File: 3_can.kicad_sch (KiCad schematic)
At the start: 6 parts, among them J301 Conn_01x04_Male, U301 TJA1441AT

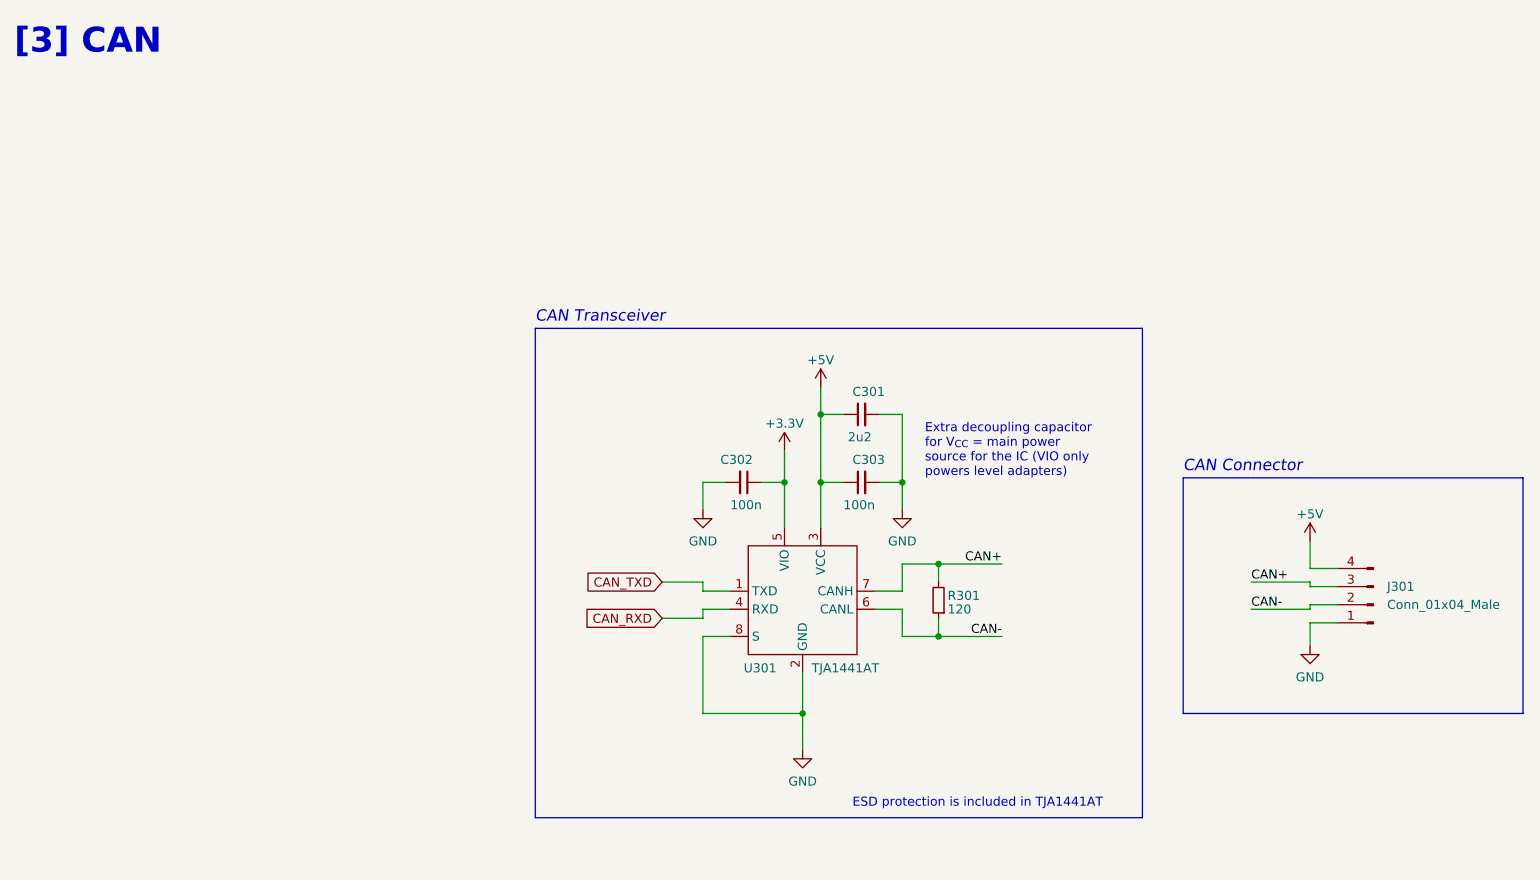
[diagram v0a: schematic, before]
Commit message: feat: major circuit rework, style update and addition of a few extra subcomponents
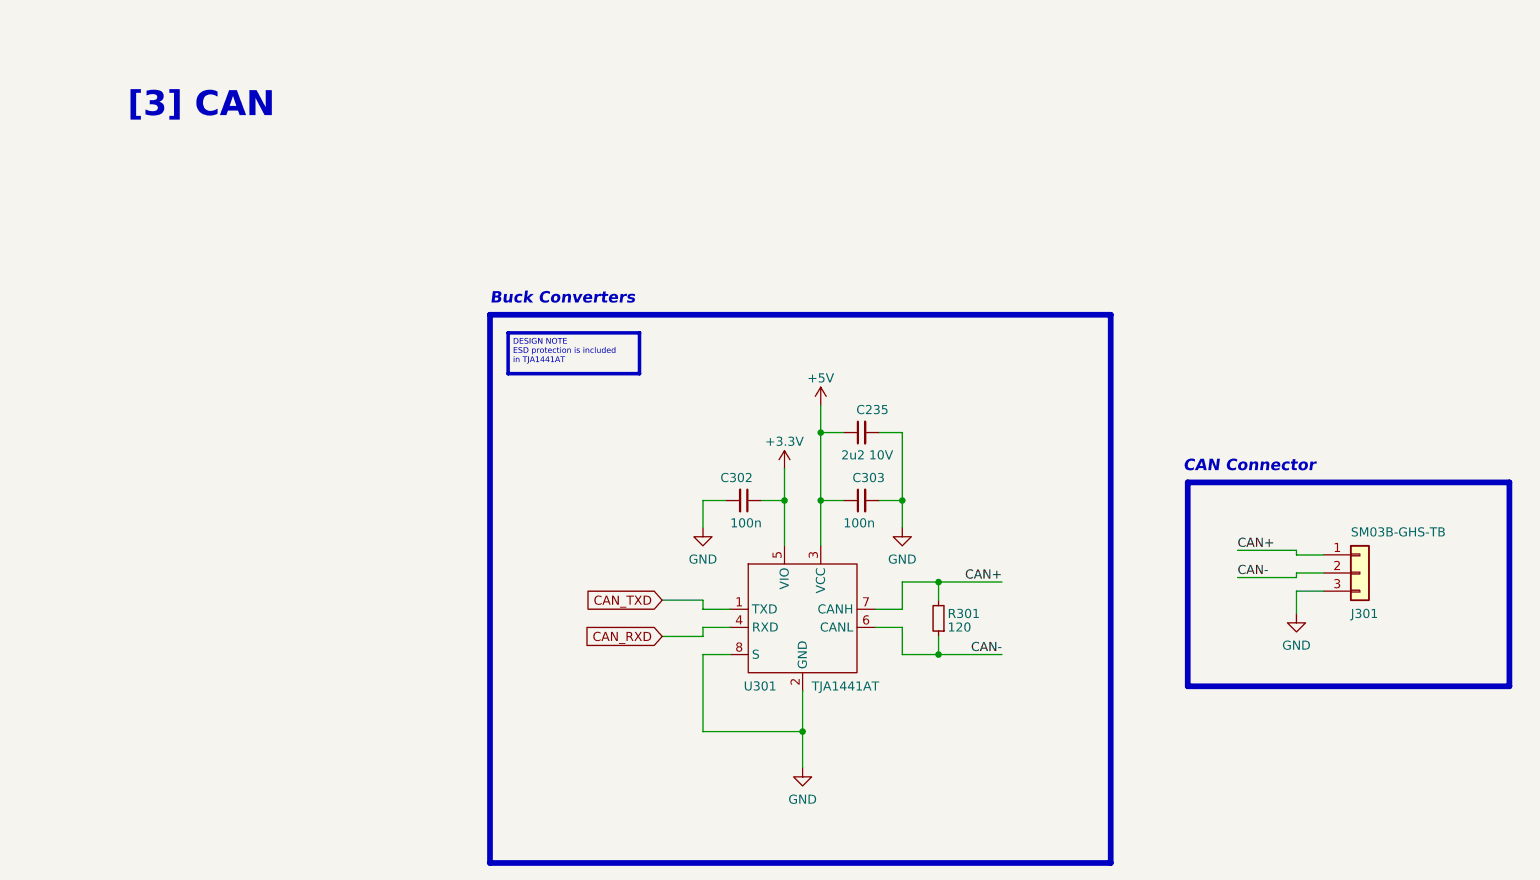
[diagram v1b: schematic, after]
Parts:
- removed C301: 2u2, Capacitor_SMD:C_0603_1608Metric_Pad1.08x0.95mm_HandSolder, symbol Device:C_Small
- removed J301: Conn_01x04_Male, Connector_PinHeader_2.54mm:PinHeader_1x04_P2.54mm_Vertical, symbol Connector:Conn_01x04_Male
- added C235: 2u2 10V, Capacitor_SMD:C_0603_1608Metric_Pad1.08x0.95mm_HandSolder, symbol Device:C_Small
- added J301: SM03B-GHS-TB, Connector_JST:JST_GH_SM03B-GHS-TB_1x03-1MP_P1.25mm_Horizontal, symbol Connector_Generic:Conn_01x03
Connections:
- net +5V: now also C235.1
- net CAN+: now also J301.1 (Pin_1)
- net CAN-: now also J301.2 (Pin_2)
- net GND: now also C235.2, J301.3 (Pin_3)
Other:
- note added: "Buck Converters"
- note removed: "CAN Transceiver"
- note removed: "ESD protection is included in TJA1441AT"
- note removed: "Extra decoupling capacitor for V_{CC} = main power source for the IC (VIO only powers level adapters)"
- moved on the sheet: C302, C303, R301, U301

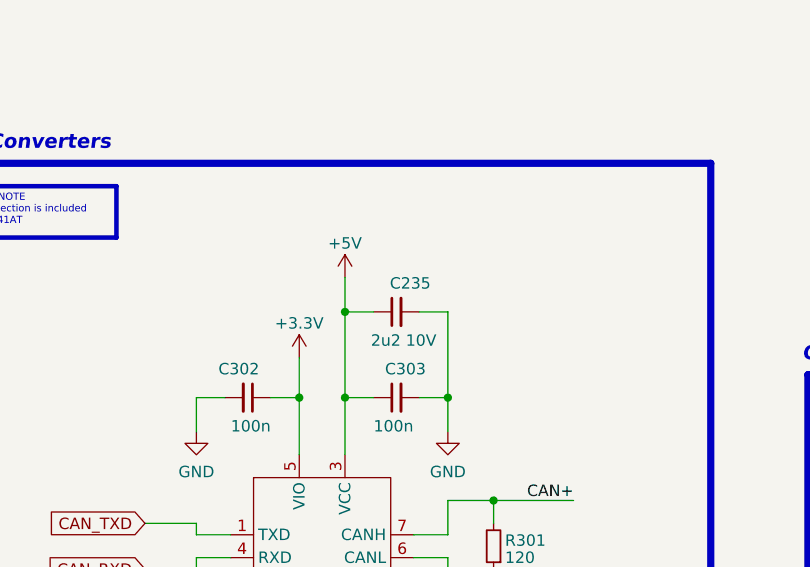
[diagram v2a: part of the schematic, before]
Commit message: feat: finished inverter placement and routing
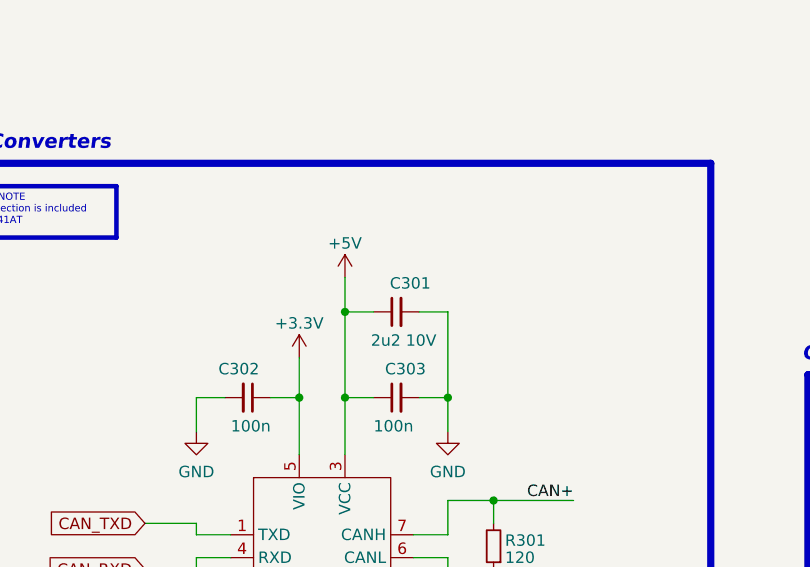
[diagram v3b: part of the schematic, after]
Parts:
- renumbered C235 to C301
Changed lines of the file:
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@@
           (reference "#PWR0139") (unit 1)
         )
-        (path "/9dea2e18-5867-4ed4-a12d-7ee109225de0/4b568fb1-3ffb-4d91-93b3-473275569108"
-          (reference "#PWR06") (unit 1)
-        )
       )
     )
@@
           (reference "#PWR0142") (unit 1)
         )
-        (path "/9dea2e18-5867-4ed4-a12d-7ee109225de0/4b568fb1-3ffb-4d91-93b3-473275569108"
-          (reference "#PWR09") (unit 1)
-        )
       )
     )
@@
   (symbol (lib_id "Device:C_Small") (at 137.16 78.105 90) (unit 1)
     (in_bom yes) (on_board yes) (dnp no)
-    (property "Reference" "C235" (at 140.97 74.93 90)
+    (property "Reference" "C301" (at 140.97 74.93 90)
       (effects (font (size 1.27 1.27)) (justify left))
     )
@@
     (instances
       (project "ESC_R1"
-        (path "/9dea2e18-5867-4ed4-a12d-7ee109225de0/bab0431c-ca33-4c57-9dbe-00ccaf05ca0f"
-          (reference "C235") (unit 1)
-        )
         (path "/9dea2e18-5867-4ed4-a12d-7ee109225de0/b6b0d34a-9e25-4b05-9733-a3c9d6720b5f"
           (reference "C301") (unit 1)
@@
           (reference "#PWR0140") (unit 1)
         )
-        (path "/9dea2e18-5867-4ed4-a12d-7ee109225de0/4b568fb1-3ffb-4d91-93b3-473275569108"
-          (reference "#PWR010") (unit 1)
-        )
       )
     )
@@
           (reference "#PWR0141") (unit 1)
         )
-        (path "/9dea2e18-5867-4ed4-a12d-7ee109225de0/4b568fb1-3ffb-4d91-93b3-473275569108"
-          (reference "#PWR08") (unit 1)
-        )
       )
     )
@@
           (reference "#PWR0138") (unit 1)
         )
-        (path "/9dea2e18-5867-4ed4-a12d-7ee109225de0/4b568fb1-3ffb-4d91-93b3-473275569108"
-          (reference "#PWR011") (unit 1)
-        )
       )
     )
@@
           (reference "C303") (unit 1)
         )
-        (path "/9dea2e18-5867-4ed4-a12d-7ee109225de0/4b568fb1-3ffb-4d91-93b3-473275569108"
-          (reference "C3") (unit 1)
-        )
       )
     )
@@
           (reference "R301") (unit 1)
         )
-        (path "/9dea2e18-5867-4ed4-a12d-7ee109225de0/4b568fb1-3ffb-4d91-93b3-473275569108"
-          (reference "R2") (unit 1)
-        )
       )
     )
@@
         (path "/9dea2e18-5867-4ed4-a12d-7ee109225de0/b6b0d34a-9e25-4b05-9733-a3c9d6720b5f"
           (reference "C302") (unit 1)
-        )
-        (path "/9dea2e18-5867-4ed4-a12d-7ee109225de0/4b568fb1-3ffb-4d91-93b3-473275569108"
-          (reference "C1") (unit 1)
         )
       )
@@
           (reference "U301") (unit 1)
         )
-        (path "/9dea2e18-5867-4ed4-a12d-7ee109225de0/4b568fb1-3ffb-4d91-93b3-473275569108"
-          (reference "U1") (unit 1)
-        )
       )
     )
@@
           (reference "#PWR0137") (unit 1)
         )
-        (path "/9dea2e18-5867-4ed4-a12d-7ee109225de0/4b568fb1-3ffb-4d91-93b3-473275569108"
-          (reference "#PWR013") (unit 1)
-        )
-      )
+      )
